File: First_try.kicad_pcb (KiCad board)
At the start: 4 copper layers, 58 x 60 mm, 139 parts, among them J1 TYPE-611-T3-W, J11 Conn_01x20, J2 Conn_01x02, J3 Conn_01x02, J4 Conn_01x06, J5 Conn_01x02, J6 Conn_01x02, J7 Conn_01x02, J9 Conn_01x20, SW1 SW_Push, SW2 SW_Push, SW3 SW_Push, SW4 SW_Push, SW6 EG1218, SW7 EG1218, U1 FT232HL-REEL, U10 20m, U11 20m, U12 TPS62240DRVR, U2 TPS62026DRCR, U3 SN74AUP2G125DCUR, U4 INA226AIDGSR, U5 INA226AIDGSR, U6 93LC56BT-I/OT, U7 ICE40UP5K-SG48I, U8 W25Q32JVSSIQ

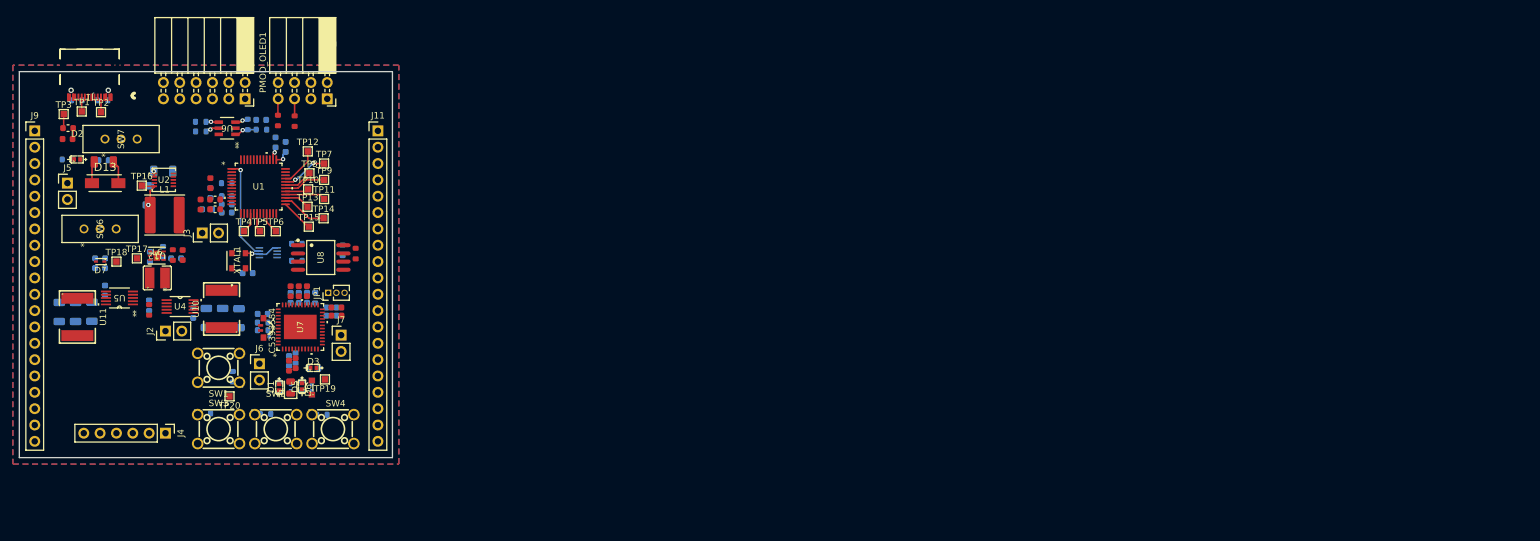
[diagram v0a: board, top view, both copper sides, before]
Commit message: Layout modifications
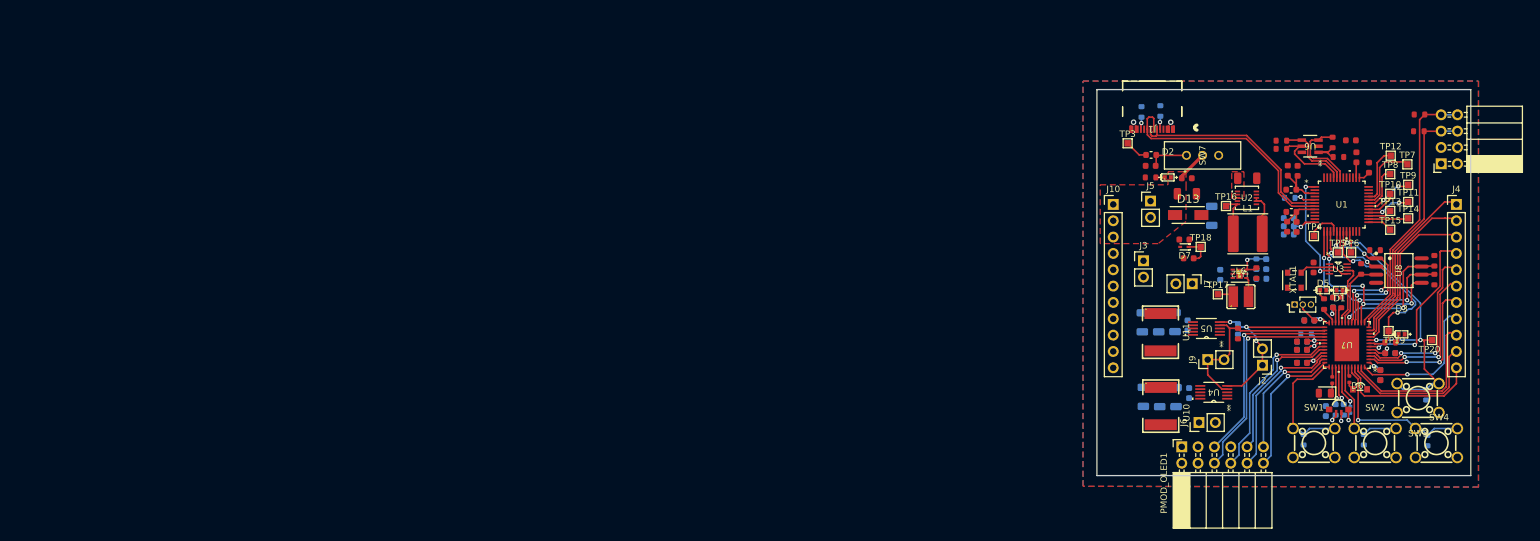
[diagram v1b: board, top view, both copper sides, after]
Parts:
- removed J11: Conn_01x20, Connector_PinHeader_2.54mm:PinHeader_1x20_P2.54mm_Vertical
- removed SW6: EG1218, footprints:SW_1218_EWI
- removed TP1, TP2: TestPoint, TestPoint:TestPoint_Pad_1.0x1.0mm
- added J10: Conn_01x11, Connector_PinHeader_2.54mm:PinHeader_1x11_P2.54mm_Vertical, F.Cu at (193.0, 40.6)
- C1, C19, C2, C22, C23, C24, C30, C31, C35, C37, C46, C48, C50, C52, C55, C57, C6, R10, R11, R15, R16, R18, R20, R28, R29, R32, R36, R37, R6, R9, U3: moved to F.Cu
- C32, C34, C4, C47, C49, C51, C53, C56: moved to B.Cu
- J4: value Conn_01x06 -> Conn_01x11; footprint Connector_PinHeader_2.54mm:PinHeader_1x06_P2.54mm_Vertical -> Connector_PinHeader_2.54mm:PinHeader_1x11_P2.54mm_Vertical
- J9: value Conn_01x20 -> Conn_01x02; footprint Connector_PinHeader_2.54mm:PinHeader_1x20_P2.54mm_Vertical -> Connector_PinHeader_2.54mm:PinHeader_1x02_P2.54mm_Vertical
- moved J4 203.8 mm to (246.4, 40.6), turned to 0 degrees
- moved TP20 187.1 mm to (242.6, 61.7)
- moved SW3 186.5 mm to (240.4, 70.7)
- moved J9 185.8 mm to (207.7, 64.8), turned to 90 degrees
- moved R8 185.5 mm to (241.7, 70.2), turned to 90 degrees
- moved R23 177.4 mm to (240.6, 26.7), turned to 180 degrees
- moved R19 174.7 mm to (240.5, 29.3), turned to 180 degrees
- moved PMOD_TMP2 173.4 mm to (244.0, 34.3), turned to 180 degrees
- moved R3 171.9 mm to (241.9, 77.3), turned to 90 degrees
- moved SW4 171.5 mm to (243.3, 77.7)
- moved SW2 170.9 mm to (233.8, 77.7)
- moved R13 170.8 mm to (222.6, 77.2), turned to 90 degrees
- moved R14 170.8 mm to (232.0, 77.2), turned to 90 degrees
- moved J2 170.6 mm to (216.2, 65.6), turned to 180 degrees
- moved SW1 170.3 mm to (224.2, 77.7)
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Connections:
- C36 pad 2: Net-(U2-FB) -> 3.3
- J1 pad A8: Net-(J1-SBU1) -> unconnected-(J1-SBU1-PadA8)
- J1 pad B8: Net-(J1-SBU2) -> unconnected-(J1-SBU2-PadB8)
- J2 pad 2: /SDA -> /SCL
- J4 pad 1: GND -> /PIN1
- J4 pad 2: /SCL_HOST -> /PIN2
- J4 pad 3: /SDA_HOST -> /PIN3
- J4 pad 4: /INT -> /PIN4
- J4 pad 5: /CE -> /PIN5
- J4 pad 6: MPPTV -> /PIN6
- J9 pad 1: +1V2 -> /SDA
- J9 pad 2: /creset -> /SDA
- L1 pad 1: Net-(U2-FB) -> 3.3
- SW1 pad 2: /button1 -> GND
- SW1 pad 3: GND -> (no net)
- SW1 pad 4: GND -> (no net)
- SW2 pad 2: /button2 -> GND
- SW2 pad 3: GND -> (no net)
- SW2 pad 4: GND -> (no net)
- SW3 pad 2: /creset -> GND
- SW3 pad 3: GND -> (no net)
- SW3 pad 4: GND -> (no net)
- SW4 pad 2: /button3 -> GND
- SW4 pad 3: GND -> (no net)
- SW4 pad 4: GND -> (no net)
- TP16 pad 1: Net-(U2-FB) -> 3.3
- U1 pad 40: +5V -> 3.3
- U2 pad 5: Net-(U2-FB) -> 3.3
- U7 pad 10: /I2C_SDA -> /PIN2
- U7 pad 11: /button1 -> /PIN1
- U7 pad 12: /button2 -> /I2C_SDA
- U7 pad 13: /button3 -> /I2C_SCL
- U7 pad 18: /SD_IO2 -> /SD_IO3
- U7 pad 19: /SD_IO3 -> /SD_IO2
- U7 pad 2: /GLED -> /PIN7
- U7 pad 20: /IOB_25b_G3 -> /FPGA_CLK
- U7 pad 21: /IOB_23b -> /GLED
- U7 pad 23: /IOT_37a -> /BLED
- U7 pad 25: /IOT_36b -> /SCL
- U7 pad 26: /IOT_39a -> /SDA
- U7 pad 27: /IOT_38b -> /PMOD_CLK
- U7 pad 28: /IOT_41a -> /VDDC
- U7 pad 3: /RLED -> /PIN6
- U7 pad 31: /IOT_42b -> /VBAT
- U7 pad 32: /IOT_43a -> /PMOD_SDO
- U7 pad 34: /IOT_44b -> /RES_PMOD
- U7 pad 35: /FPGA_CLK -> unconnected-(U7-IOT_46b_G0-Pad35)
- U7 pad 36: /VDDC -> /DC_PMOD
- U7 pad 37: /IOT_45a_G1 -> /button1
- U7 pad 38: /VBAT -> /RLED
- U7 pad 4: /BLED -> /PIN5
- U7 pad 42: /RES_PMOD -> /button2
- U7 pad 43: /DC_PMOD -> /OLED
- U7 pad 44: /PMOD_CLK -> /button3
- U7 pad 45: /PMOD_SDO -> /PIN11
- U7 pad 46: /PMOD_SS -> /PIN10
- U7 pad 47: /SCL -> /PIN9
- U7 pad 48: /SDA -> /PIN8
- U7 pad 6: /OLED -> /PIN4
- U7 pad 9: /I2C_SCL -> /PIN3
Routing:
- net /creset: track 0.00 -> 47.7 mm, vias 0 -> 3
- net /I2C_SCL: track 2.57 -> 41.4 mm
- net /D_P: track 0.00 -> 38.0 mm
- net /I2C_SDA: track 2.65 -> 39.2 mm
- net /SCK: track 0.00 -> 34.0 mm, vias 0 -> 3
- net /D_M: track 0.00 -> 33.9 mm
- net /VDDC: track 0.00 -> 33.6 mm, vias 0 -> 1
- net /PMOD_CLK: track 0.00 -> 31.9 mm, vias 0 -> 1
- net /SDO: track 0.00 -> 31.7 mm, vias 0 -> 4
- net /SDA: track 0.00 -> 30.8 mm
- net /SCL: track 0.00 -> 30.4 mm, vias 0 -> 3
- net /cdone: track 0.00 -> 30.2 mm, vias 0 -> 2
- net /VBAT: track 0.00 -> 27.8 mm, vias 0 -> 1
- net /PIN1: track 0.00 -> 27.2 mm
- net /PIN5: track 0.00 -> 27.0 mm, vias 0 -> 2
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- added copper zone on F.Cu, net +5V
- added copper zone on In1.Cu, net GND
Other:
- board size 58 x 60 mm -> 58.1 x 60 mm
- board text added: "${REFERENCE}"

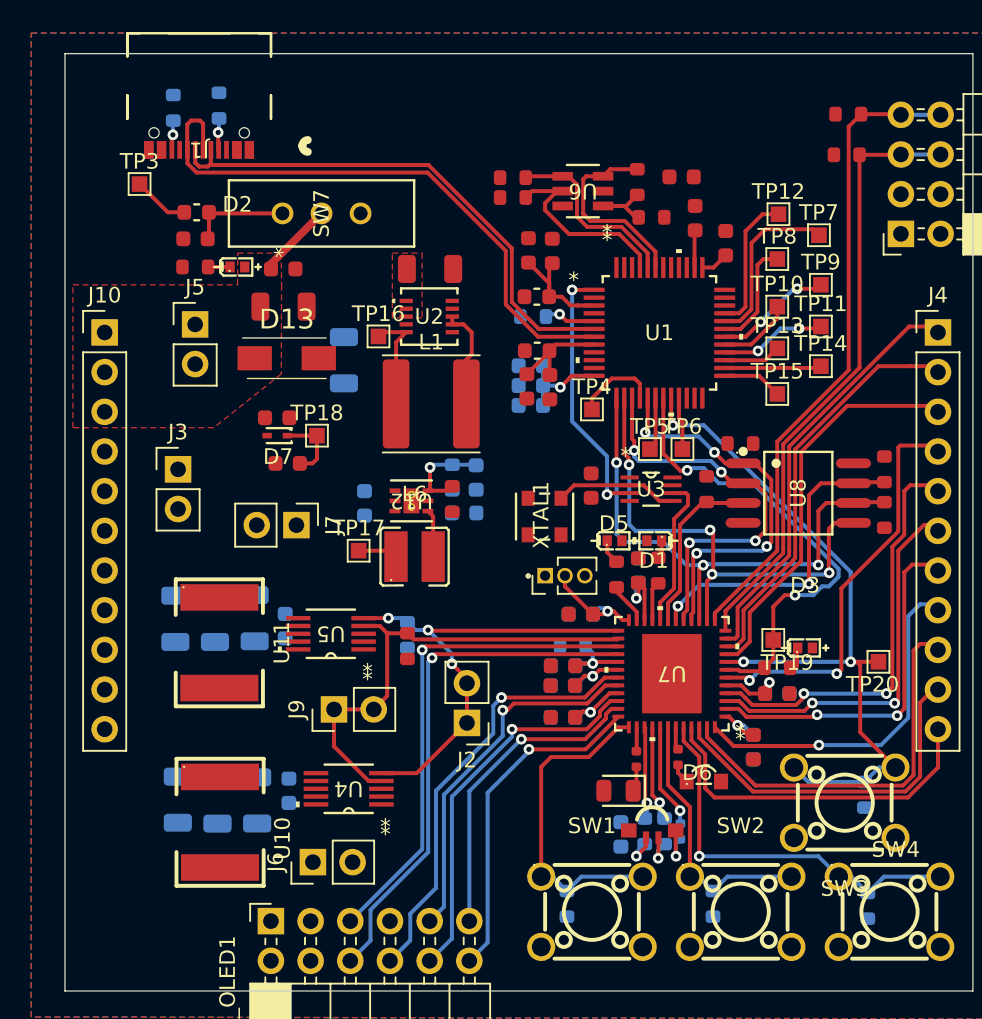
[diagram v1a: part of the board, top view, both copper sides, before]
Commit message: Layout modifications
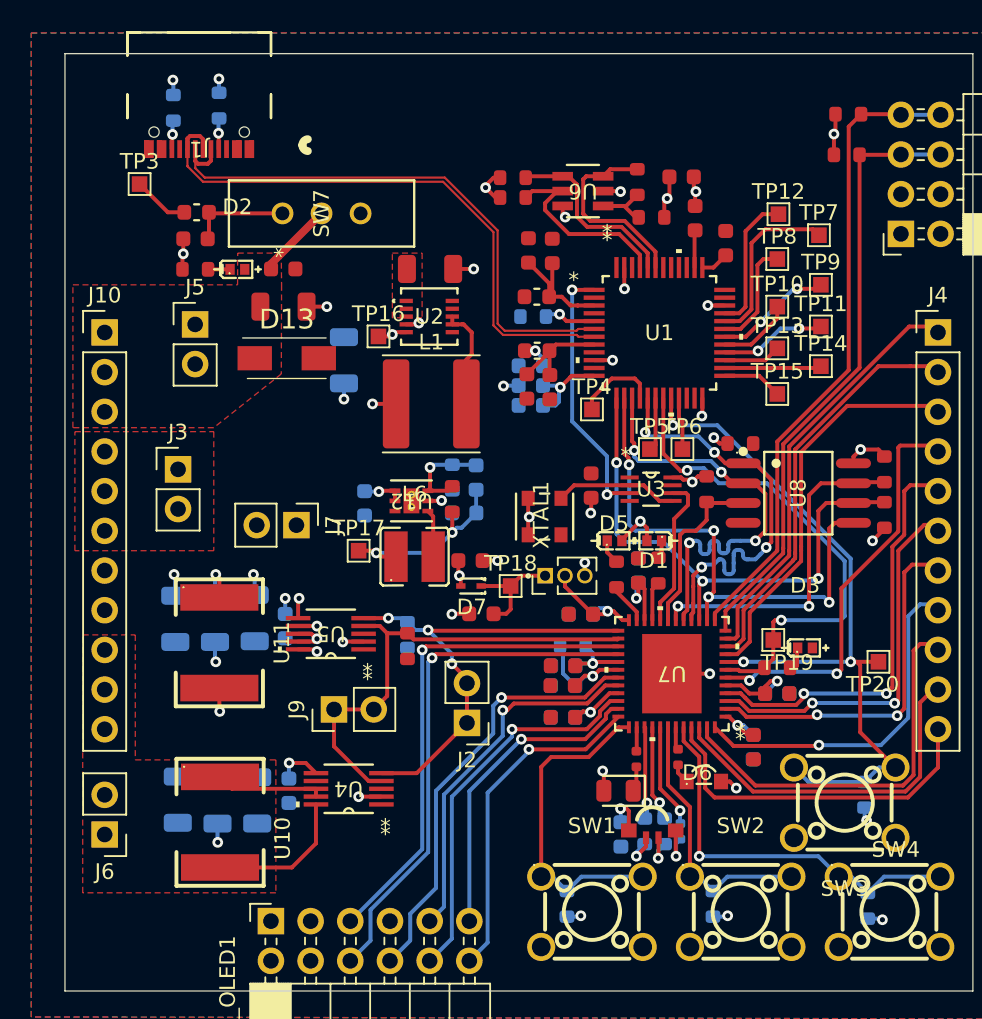
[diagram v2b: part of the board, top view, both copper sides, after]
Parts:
- moved C2 15.7 mm to (217.2, 58.6)
- moved D7 15.7 mm to (216.5, 56.9)
- moved TP18 15.7 mm to (219.0, 56.9)
- moved C1 15.4 mm to (216.5, 55.2)
- moved J6 13.4 mm to (193.0, 72.8), turned to 180 degrees
- moved D2 0.15 mm to (201.5, 36.6)
- moved R6 0.15 mm to (198.8, 36.6)
- moved J1 0.05 mm to (199.1, 25.2)
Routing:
- net +3V3: track 12.8 -> 54.1 mm, vias 3 -> 27
- net GND: track 0.00 -> 24.8 mm, vias 0 -> 19
- net 1.2: track 2.55 -> 23.0 mm, vias 0 -> 2
- net 3.3: track 12.9 -> 27.6 mm, vias 1 -> 14
- net +1V2: track 9.01 -> 19.7 mm
- net /D_M: track 33.9 -> 36.5 mm
- net /SDO: track 31.7 -> 34.2 mm
- net +2V5: track 4.59 -> 7.07 mm
- net /SDI: track 26.6 -> 29.0 mm
- net /cdone: track 30.2 -> 32.2 mm
- net /SS: track 25.1 -> 26.8 mm
- net /SD_IO3: track 20.8 -> 21.6 mm
- net /creset: track 47.7 -> 48.2 mm
- added copper zone on F.Cu, net +1V2
- added copper zone on In2.Cu, net +1V2
- added copper zone on F.Cu, net +3V3
- added copper zone on In2.Cu, net +3V3

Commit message: Last version
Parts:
- removed PMOD_OLED1: Conn_02x06_Top_Bottom, Connector_PinSocket_2.54mm:PinSocket_2x06_P2.54mm_Horizontal
- removed PMOD_TMP2: Conn_02x04_Top_Bottom, Connector_PinSocket_2.54mm:PinSocket_2x04_P2.54mm_Horizontal
- removed R3: 10kΩ, PCM_JLCPCB:R_0603
- removed SW4: SW_Push, footprints:SW_push
- removed U12: TPS62240DRVR, footprints:Vreg1_2
- added R14: 10kΩ, PCM_JLCPCB:R_0603, B.Cu at (241.6, 77.1)
- added REF**: Vreg1_2, footprints:Vreg1_2, F.Cu at (212.8, 51.4)
- added REF**: PinSocket_2x06_P2.54mm_Horizontal_edit, footprints:PinSocket_2x06_P2.54mm_Horizontal_edit, F.Cu at (203.7, 78.4)
- added REF**: PinSocket_2x04_P2.54mm_Horizontal_edit, footprints:PinSocket_2x04_P2.54mm_Horizontal_edit, F.Cu at (244.5, 34.4)
- added SW2: SW_Push, footprints:SW_push, F.Cu at (243.4, 77.7)
- J1: footprint footprints:C_conn -> Connector_USB:USB_C_Receptacle_HCTL_HC-TYPE-C-16P-01A
- moved C6 3.95 mm to (221.8, 53.6), turned to 0 degrees
- moved OSC 1.86 mm to (222.3, 51.0)
- moved C40 1.46 mm to (197.7, 69.1)
- moved C41 1.46 mm to (200.3, 69.1)
- moved U10 1.46 mm to (200.4, 70.5)
- moved C42 1.46 mm to (202.8, 69.1)
- moved R37 1.40 mm to (234.7, 46.7)
- moved R2 0.97 mm to (198.1, 25.6)
- moved D3 0.72 mm to (238.4, 60.3)
- moved R1 0.71 mm to (199.9, 25.6)
- moved TP10 0.68 mm to (236.8, 39.0)
- moved TP12 0.68 mm to (236.9, 33.1)
- moved TP13 0.68 mm to (236.8, 41.7)
- moved TP15 0.68 mm to (236.8, 44.6)
- moved TP8 0.68 mm to (236.8, 35.9)
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- renumbered XTAL1 to OSC
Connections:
- SW1 pad 2: GND -> /button1
- SW1 pad 3: (no net) -> GND
- SW1 pad 4: (no net) -> GND
- SW2 pad 2: GND -> /button2
- SW2 pad 3: (no net) -> GND
- SW2 pad 4: (no net) -> GND
- SW3 pad 1: /creset -> GND
- SW3 pad 3: (no net) -> /creset
- SW3 pad 4: (no net) -> /creset
- U7 pad 35: unconnected-(U7-IOT_46b_G0-Pad35) -> /PMOD_SS
- U7 pad 44: /button3 -> button3
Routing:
- net GND: track 24.8 -> 83.3 mm, vias 19 -> 39
- net +1V2: track 19.7 -> 50.8 mm, vias 2 -> 3
- net 3.3: track 27.6 -> 54.2 mm
- net /button3: track 25.5 -> 0.00 mm, vias 1 -> 0
- net button3: track 0.00 -> 23.0 mm
- net 1.2: track 23.0 -> 42.6 mm
- net Net-(J1-VBUS-PadA4): track 3.61 -> 14.0 mm
- net +3V3: track 54.1 -> 62.3 mm
- net +5V: track 4.90 -> 12.4 mm
- net /SS: track 26.8 -> 29.8 mm
- net Net-(D3-K): track 1.66 -> 3.10 mm
- net Net-(OSC1-OUTPUT): track 7.90 -> 6.66 mm
- net Net-(J1-CC2): track 1.86 -> 2.91 mm
- net Net-(U1-ACBUS6): track 7.53 -> 8.57 mm
- net /D_M: track 36.5 -> 37.4 mm
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- added copper zone on In2.Cu, net 3.3
- removed copper zone on F.Cu, net +3V3
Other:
- board size 58.1 x 60 mm -> 58.1 x 62.5 mm
- board text added: "+3V3"
- board text added: "1.2"
- board text added: "3.3"
- board text added: "5V"
- board text added: "GND"
- board text added: "Moraru Anastasia"
- board text added: "SCL"
- board text added: "SDA"
- board text added: "reset"
- board text removed: "${REFERENCE}"

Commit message: RISC-V added
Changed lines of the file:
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@@
 	)
 	(segment
-		(start 227.5986 65.9122)
-		(end 227.641 65.9546)
-		(width 0.254)
-		(layer "F.Cu")
-		(net 58)
-	)
-	(segment
-		(start 227.641 65.9546)
+		(start 227.751857 70.762361)
 		(end 227.641 70.651504)
 		(width 0.254)
@@
 	(segment
 		(start 227.641 70.651504)
+		(end 227.641 65.9546)
+		(width 0.254)
+		(layer "F.Cu")
+		(net 58)
+	)
+	(segment
+		(start 227.751857 70.8)
 		(end 227.751857 70.762361)
 		(width 0.254)
@@
 		(net 58)
 	)
+	(segment
+		(start 227.641 65.9546)
+		(end 227.5986 65.9122)
+		(width 0.254)
+		(layer "F.Cu")
+		(net 58)
+	)
 	(via
-		(at 227.751857 70.762361)
+		(at 227.751857 70.8)
 		(size 0.6858)
 		(drill 0.3302)
@@
 	)
 	(segment
-		(start 227.751857 70.762361)
+		(start 227.751857 70.8)
 		(end 227.751857 71.611143)
 		(width 0.254)
